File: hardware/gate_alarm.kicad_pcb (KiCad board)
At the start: 2 copper layers, 40.6 x 64.8 mm, 8 parts, among them U1 ATtiny212-SS, U2 NodeMCU_1.0_(ESP-12E), U3 NCP718, U4 AH9250

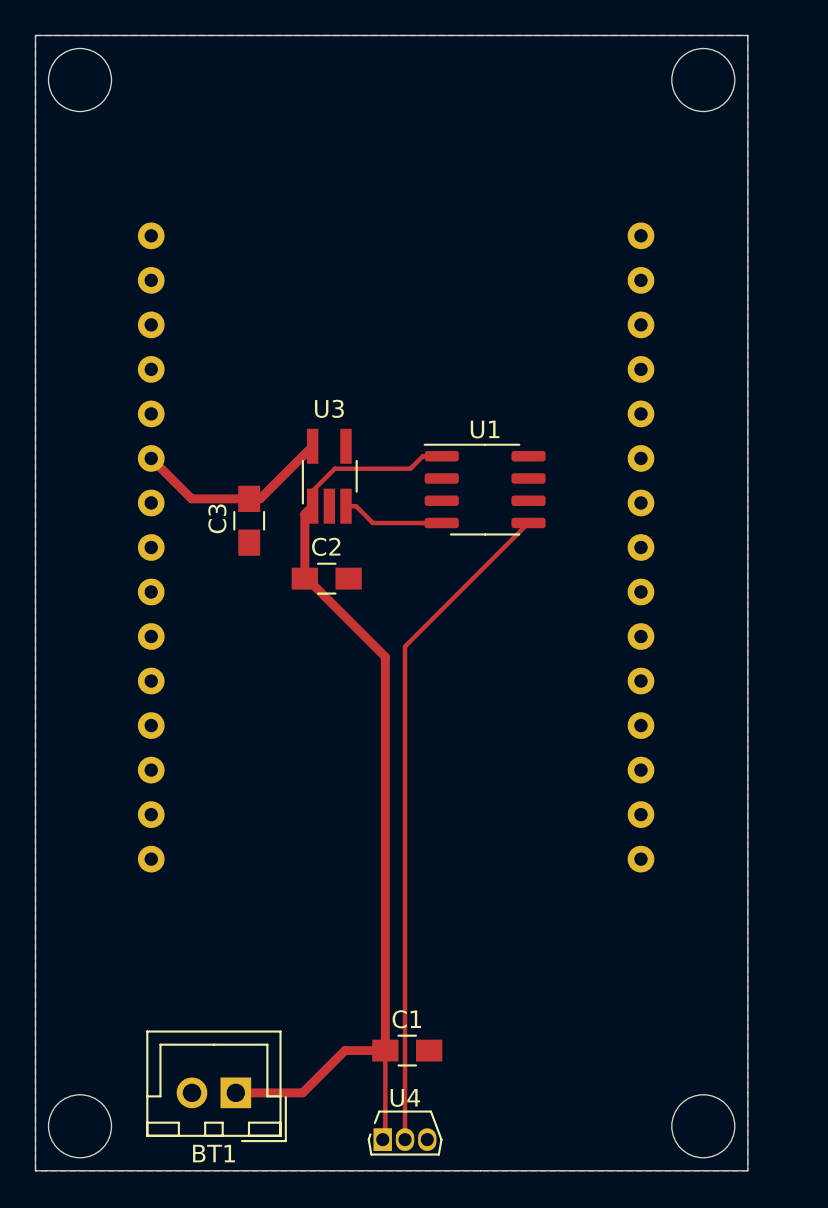
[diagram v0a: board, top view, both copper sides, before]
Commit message: Update hardware for first PCB manufacture
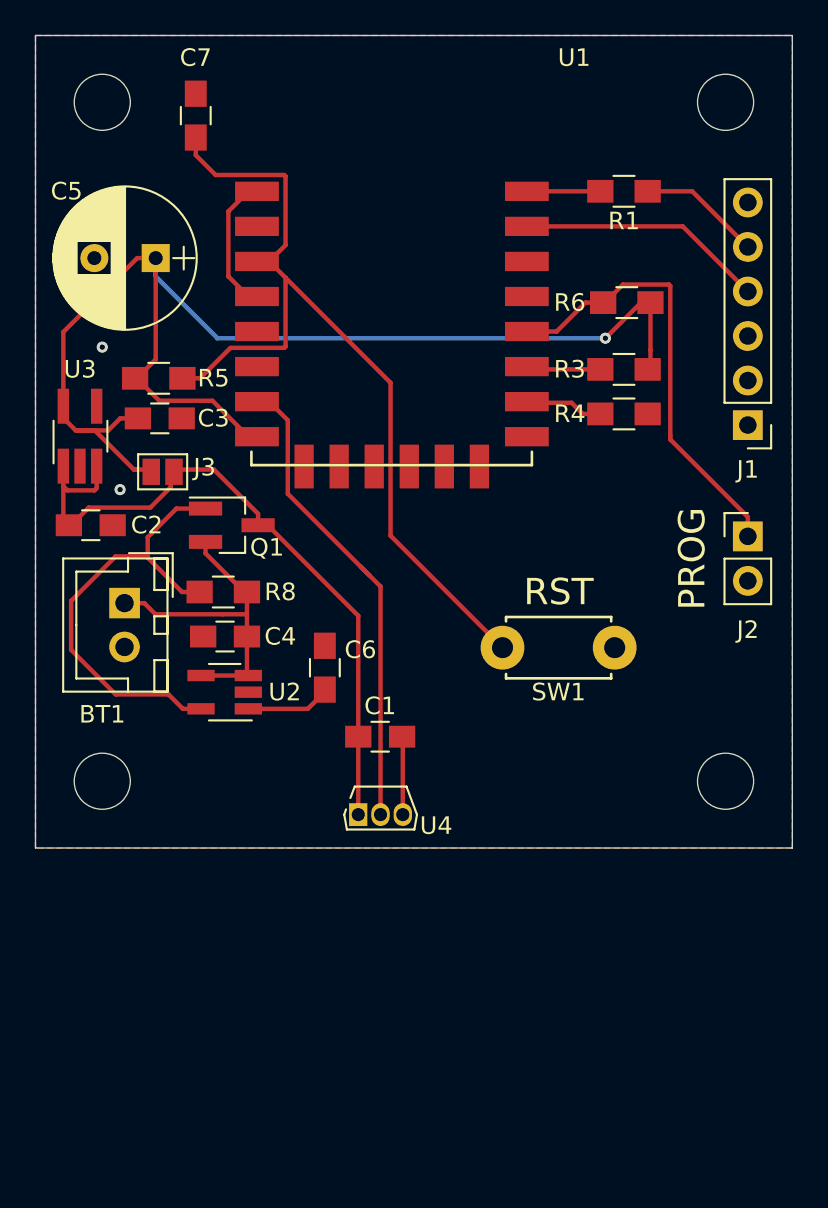
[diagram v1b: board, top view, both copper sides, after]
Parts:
- added C4: 100n, Capacitors_SMD:C_0805_HandSoldering, F.Cu at (32.4, 57.1)
- added C5: 1000u, Capacitors_THT:CP_Radial_D8.0mm_P3.50mm, F.Cu at (28.4, 35.6)
- added C6: NC, Capacitors_SMD:C_0805_HandSoldering, F.Cu at (38.1, 58.9)
- added C7: 100n, Capacitors_SMD:C_0805_HandSoldering, F.Cu at (30.7, 27.4)
- added J1: Conn_01x06_Male, Pin_Headers:Pin_Header_Straight_1x06_Pitch2.54mm, F.Cu at (62.2, 45.1)
- added J2: Conn_01x02_Male, Pin_Headers:Pin_Header_Straight_1x02_Pitch2.54mm, F.Cu at (62.2, 51.4)
- added J3: Jumper, Jumpers:SolderJumper-2_P1.3mm_Open_Pad1.0x1.5mm, F.Cu at (28.8, 47.8)
- added Q1: AO3415, TO_SOT_Packages_SMD:SOT-23_Handsoldering, F.Cu at (32.8, 50.8)
- added R1: 499R, Resistors_SMD:R_0805_HandSoldering, F.Cu at (55.2, 31.8)
- added R3: 10k, Resistors_SMD:R_0805_HandSoldering, F.Cu at (55.2, 41.9)
- added R4: 10k, Resistors_SMD:R_0805_HandSoldering, F.Cu at (55.2, 44.5)
- added R5: 10k, Resistors_SMD:R_0805_HandSoldering, F.Cu at (28.6, 42.4)
- added R6: 10k, Resistors_SMD:R_0805_HandSoldering, F.Cu at (55.3, 38.1)
- added R8: 330k, Resistors_SMD:R_0805_HandSoldering, F.Cu at (32.3, 54.6)
- added REF**: MountingHole_3.2mm_M3, Mounting_Holes:MountingHole_3.2mm_M3, F.Cu at (61.0, 26.7)
- added REF**: MountingHole_3.2mm_M3, Mounting_Holes:MountingHole_3.2mm_M3, F.Cu at (25.4, 26.7)
- added REF**: MountingHole_3.2mm_M3, Mounting_Holes:MountingHole_3.2mm_M3, F.Cu at (25.4, 65.4)
- added REF**: MountingHole_3.2mm_M3, Mounting_Holes:MountingHole_3.2mm_M3, F.Cu at (61.0, 65.4)
- added SW1: SW_MEC, custom_switches:PTS636_THT, F.Cu at (51.4, 57.8)
- C1, C2, C3: value 0.1u -> 100n
- U1: value ATtiny212-SS -> ESP-12F; footprint Package_SO:SOIC-8_3.9x4.9mm_P1.27mm -> ESP8266:ESP-12E_SMD
- U2: value NodeMCU_1.0_(ESP-12E) -> LP3470A; footprint ESP8266:NodeMCU1.0(12-E) -> TO_SOT_Packages_SMD:SOT-23-5_HandSoldering; moved to F.Cu
- moved BT1 28.7 mm to (26.7, 55.2), turned to 270 degrees
- moved U1 21.0 mm to (34.9, 31.8)
- moved U4 18.6 mm to (40.0, 67.3)
- moved C1 18.0 mm to (41.3, 62.9)
- moved U3 14.4 mm to (24.1, 45.7)
- moved C2 13.8 mm to (24.7, 50.8)
- moved U2 12.8 mm to (32.4, 60.3)
- moved C3 7.75 mm to (28.7, 44.7), turned to 0 degrees
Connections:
- BT1 pad 1: +BATT -> Net-(BT1-Pad1)
- U1 pad 1: +BATT -> Net-(U1-Pad1)
- U1 pad 3: (no net) -> /~RESET
- U1 pad 4: /RUN8266 -> Net-(U1-Pad1)
- U1 pad 5: /~GATE_OPEN -> (no net)
- U1 pad 7: (no net) -> /~GATE_OPEN
- U1 pad 8: GND -> +3V3
- U2 pad 1: (no net) -> Net-(C6-Pad1)
- U2 pad 2: (no net) -> GND
- U2 pad 3: (no net) -> Net-(BT1-Pad1)
- U2 pad 4: (no net) -> Net-(BT1-Pad1)
- U2 pad 5: (no net) -> Net-(Q1-Pad1)
- U3 pad 3: /RUN8266 -> +BATT
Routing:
- net +3V3: track 11.4 -> 75.5 mm, vias 0 -> 1
- net /~RESET: track 0.00 -> 50.0 mm
- net /~PROG: track 0.00 -> 26.1 mm
- net Net-(Q1-Pad1): track 0.00 -> 26.0 mm
- net Net-(BT1-Pad1): track 0.00 -> 18.7 mm
- net +BATT: track 56.9 -> 40.4 mm
- net /UART_RX: track 0.00 -> 14.8 mm
- net /~GATE_OPEN: track 38.1 -> 26.9 mm
- net Net-(U1-Pad1): track 0.00 -> 9.32 mm
- net /UART_TX: track 0.00 -> 7.03 mm
- net /RUN8266: track 5.86 -> 0.00 mm
- net Net-(R4-Pad2): track 0.00 -> 5.18 mm
- net Net-(R3-Pad1): track 0.00 -> 4.96 mm
- net Net-(C6-Pad1): track 0.00 -> 4.89 mm
- net Net-(R1-Pad2): track 0.00 -> 4.89 mm
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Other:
- board size 40.6 x 64.8 mm -> 43.2 x 46.4 mm
- net class Default: clearance 0.1524 -> 0.254
- rule trace_clearance: 0.1524 -> 0.254
- board text added: "PROG"
- board text added: "RST"
